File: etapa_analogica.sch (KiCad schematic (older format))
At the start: 50 parts

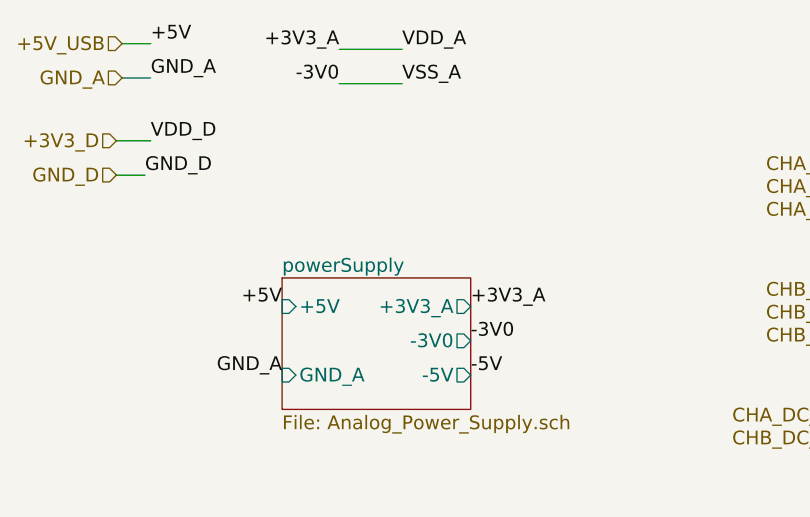
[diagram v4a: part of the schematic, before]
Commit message: New version of mainboard. Corrected errors and modified analog part.
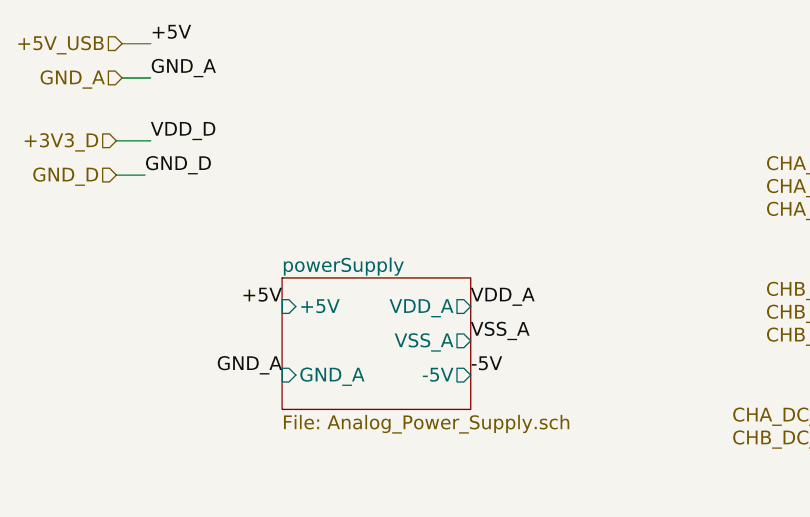
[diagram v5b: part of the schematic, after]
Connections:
- net labels removed: +3V3_A, -3V0
- wire segments 152 -> 150
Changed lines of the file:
@@
 F1 "Analog_Power_Supply.sch" 60
 F2 "+5V" I L 1900 1825 60
-F3 "-3V0" O R 2725 1975 60
-F4 "GND_A" I L 1900 2125 60
-F5 "-5V" O R 2725 2125 60
-F6 "+3V3_A" O R 2725 1825 60
+F3 "GND_A" I L 1900 2125 60
+F4 "-5V" O R 2725 2125 60
+F5 "VDD_A" O R 2725 1825 60
+F6 "VSS_A" O R 2725 1975 60
 $EndSheet
 $Sheet
@@
 Text Label 1325 675  0    60   ~ 0
 +5V
-Text Label 2150 700  2    60   ~ 0
-+3V3_A
-Text Label 2150 850  2    60   ~ 0
--3V0
-Text Label 2425 700  0    60   ~ 0
+Text Label 2725 1825 0    60   ~ 0
 VDD_A
-Text Label 2425 850  0    60   ~ 0
+Text Label 2725 1975 0    60   ~ 0
 VSS_A
 Text Label 8925 2150 2    60   ~ 0
@@
 Text Label 1900 1825 2    60   ~ 0
 +5V
-Text Label 2725 1825 0    60   ~ 0
-+3V3_A
-Text Label 2725 1975 0    60   ~ 0
--3V0
 Text Label 2725 2125 0    60   ~ 0
 -5V
@@
 	1200 675  1325 675
 Wire Wire Line
-	2150 850  2425 850
-Wire Wire Line
-	2150 700  2425 700
-Wire Wire Line
 	1175 1100 1325 1100
